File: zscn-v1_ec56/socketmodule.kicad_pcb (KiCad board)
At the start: 2 copper layers, 53 x 66 mm, 3 parts, among them J1 EC56-L-02x14, J2 Conn_02x32_Counter_Clockwise, J4 EC56-R-02x14

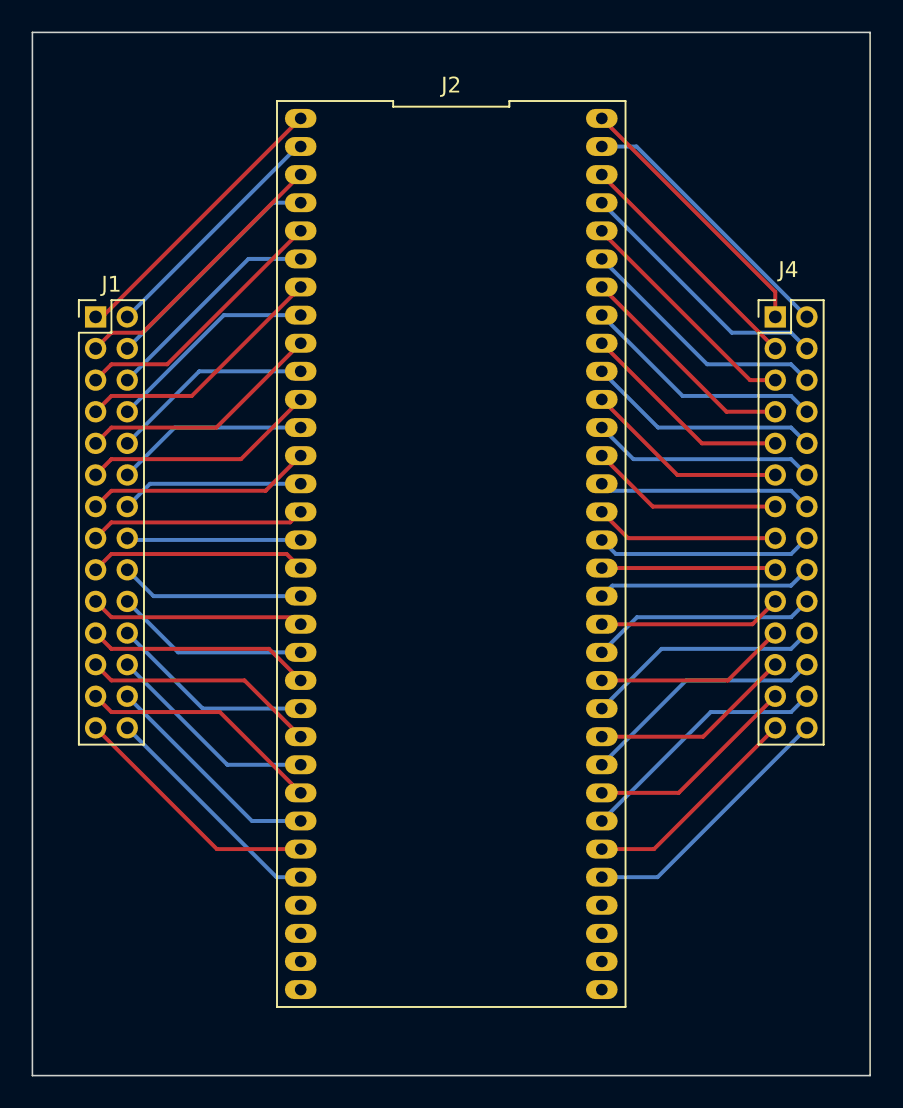
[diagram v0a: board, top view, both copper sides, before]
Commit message: fixed spacing issues rev 2
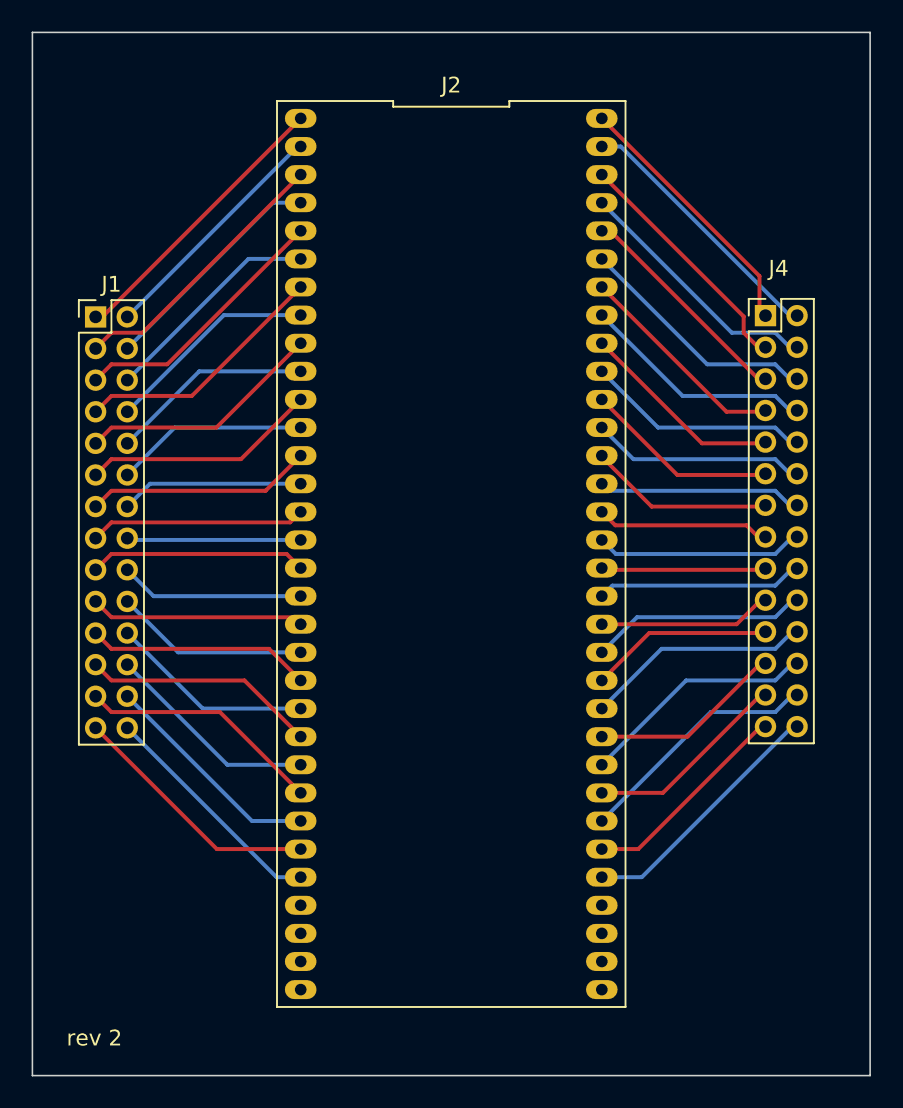
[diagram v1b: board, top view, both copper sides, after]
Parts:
- moved J4 0.63 mm to (142.4, 79.9)
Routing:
- net /R12: track 14.2 -> 13.2 mm
- net /R20: track 14.3 -> 13.3 mm
- net /R10: track 14.9 -> 13.9 mm
- net /R9: track 13.6 -> 12.6 mm
- net /R8: track 15.5 -> 14.5 mm
- net /R7: track 14.2 -> 13.2 mm
- net /R6: track 16.2 -> 15.2 mm
- net /R28: track 16.9 -> 15.9 mm
- net /R27: track 14.2 -> 13.2 mm
- net /R25: track 13.5 -> 12.5 mm
- net /R24: track 15.6 -> 14.6 mm
- net /R23: track 12.9 -> 11.9 mm
- net /R21: track 12.2 -> 11.2 mm
- net /R2: track 17.4 -> 16.4 mm
- net /R19: track 11.6 -> 10.6 mm
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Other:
- board text added: "rev 2"
